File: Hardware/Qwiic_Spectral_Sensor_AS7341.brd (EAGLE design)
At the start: 25.4 x 25.4 mm, 43 parts, among them J1 QWIIC_RIGHT_ANGLE, J3 QWIIC_RIGHT_ANGLE, U1 MLX90614

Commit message: Working on schematic
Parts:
- removed R5: 2.2k, SparkFun-Resistors:0603
- added C2: 0.1uF, SparkFun-Capacitors:0603
- added C3, C4: 1.0uF, SparkFun-Capacitors:0603
- added D2: White, 60mA, SparkFun-LED:SUPER_BRIGHT_SMD_LED_3014
- added D3: LED-IR0603, SparkFun-LED:LED-0603
- added D4, D5: (no value), SparkFun-LED:LED_3MM-NS
- added JP3, JP4: JUMPER-SMT_2_NC_TRACE_SILK, SparkFun-Jumpers:SMT-JUMPER_2_NC_TRACE_SILK
- added R1: 2.2k, SparkFun-Resistors:0603
- added U2: PCA9536, New_Parts:MSOP8
- added U3: AP2127K-1.8V, SparkFun-IC-Power:SOT23-5
- C1: value 0.1uF -> 10uF
- U1: value MLX90614 -> AS7341OLGA; device SparkFun-Sensors:TO-39 -> AS7341:OLGA8
- moved R2 54.4 mm to (-14.0, -26.7)
- moved JP1 48.5 mm to (-8.89, -17.8), flipped to the top, turned to 0 degrees
- moved C1 25.6 mm to (-3.81, -15.2), turned to 0 degrees
- moved U1 24.3 mm to (-3.81, -5.08)
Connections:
- new net 1.8V: C4.1, U1.1, U3.5
- new net GPIO0: U2.1
- new net GPIO1: U2.2
- new net GPIO2: U2.3
- new net GPIO3: U2.5
- new net LDR: D2.C, D3.C, D4.K, D5.K, U1.4
- new net N$5: D2.A, JP4.1
- new net N$6: U3.1, U3.3
- new net N$7: D3.A, JP3.1
- net 3.3V: now also C2.1, C3.1, U2.8; no longer U1.3
- net GND: now also C2.2, C3.2, C4.2, U1.3, U1.5, U2.4, U3.2; no longer U1.4
- net N$1: now also JP1.3, R1.1; no longer JP1.1, R2.2
- net N$3: now also JP1.1, R2.1; no longer JP1.3, R5.2
- net SCL: now also R2.2, U1.2, U2.6; no longer R2.1, U1.1
- net SDA: now also R1.2, U1.8, U2.7; no longer R5.1, U1.2
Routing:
- net 3.3V: track 48.2 -> 31.1 mm
- net SDA: track 38.4 -> 29.1 mm
- net SCL: track 44.4 -> 39.4 mm
- net N$1: track 4.36 -> 0.00 mm, vias 1 -> 0
- net N$3: track 4.32 -> 0.00 mm, vias 1 -> 0

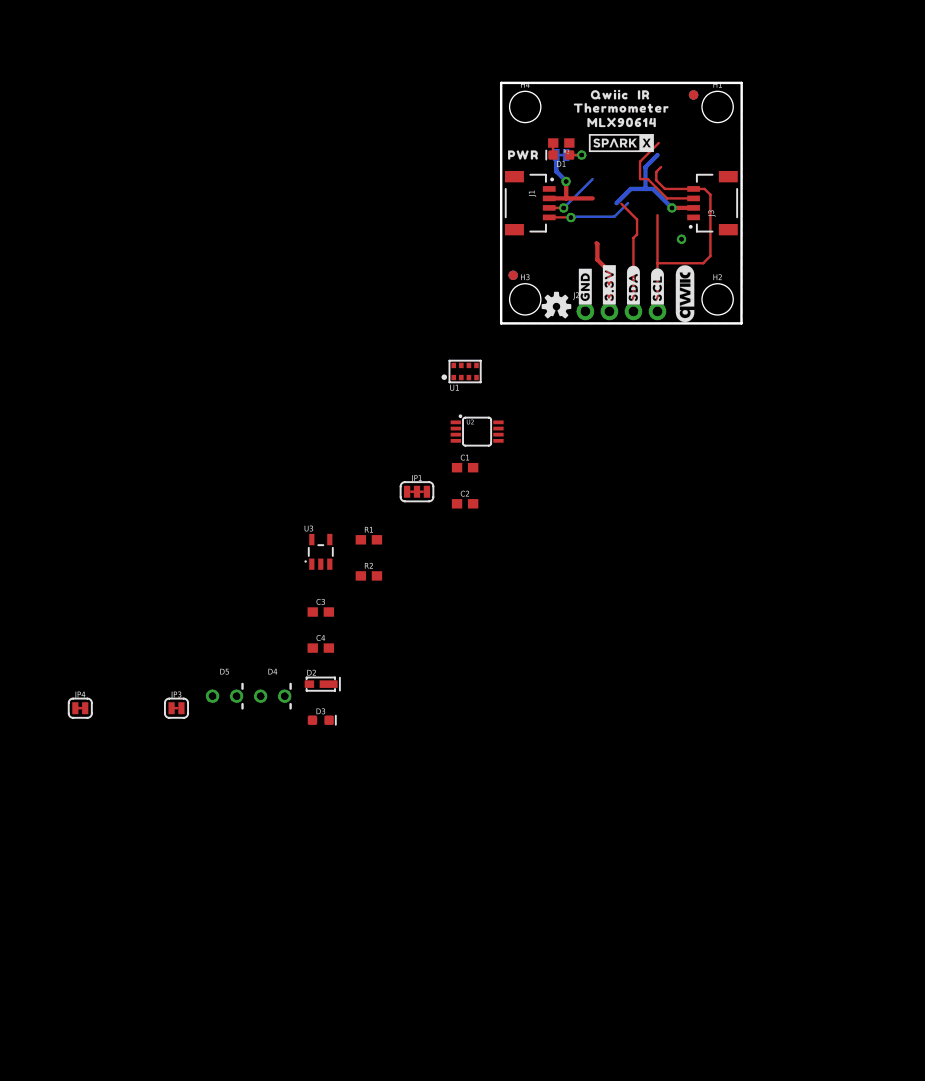
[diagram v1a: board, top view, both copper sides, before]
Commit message: First draft of schematic finished
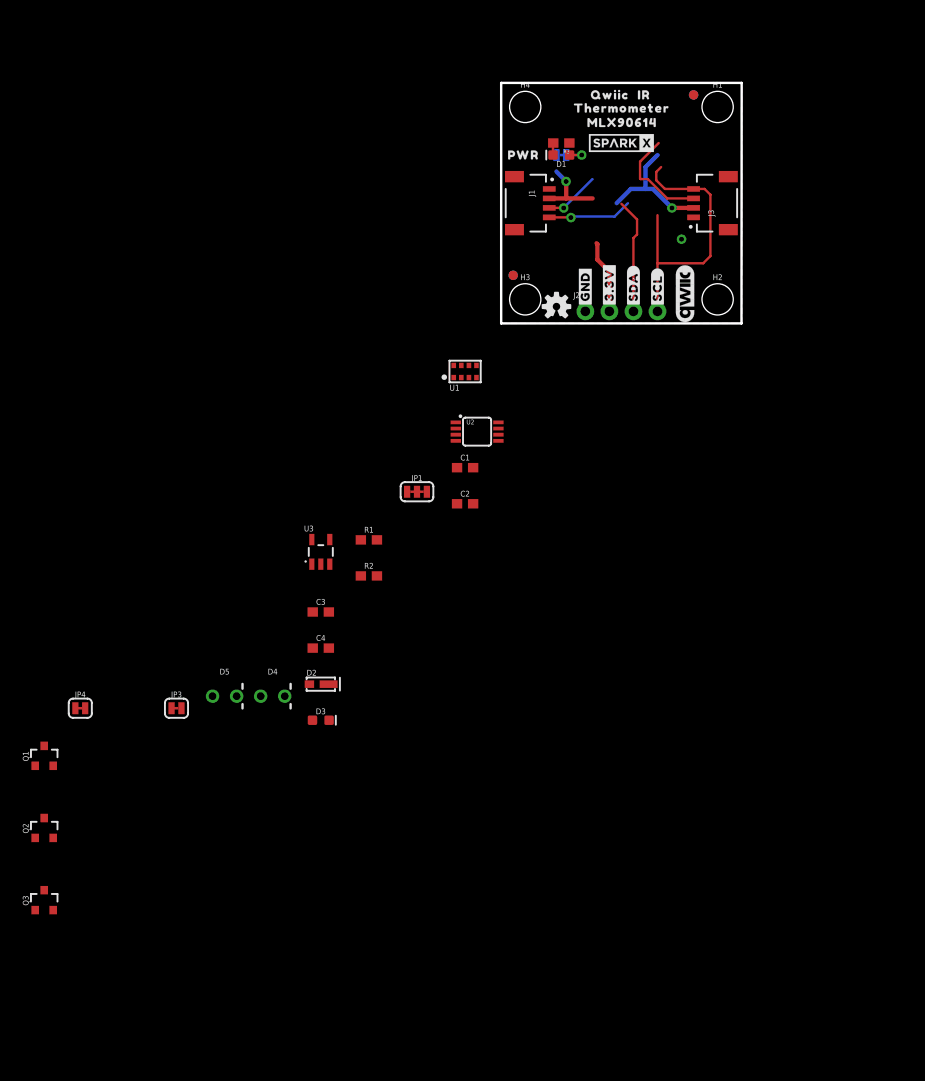
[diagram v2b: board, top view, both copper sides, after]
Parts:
- added Q1, Q2, Q3: 20V/4.2A/52mΩ/1.4W, SparkFun-DiscreteSemi:SOT23-3
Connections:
- new net N$10: JP2.2, Q3.2
- new net N$8: D4.A, JP4.2, Q1.2
- new net N$9: D5.A, JP3.2, Q2.2
- net 3.3V: now also Q1.3, Q2.3, Q3.3; no longer JP2.2
- net GPIO0: now also Q3.1
- net GPIO1: now also Q1.1
- net GPIO2: now also Q2.1
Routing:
- net 3.3V: track 31.1 -> 29.3 mm
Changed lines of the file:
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@@
 <attribute name="VALUE" x="-44.45" y="-41.783" size="0.6096" layer="27" font="vector" ratio="20" align="top-center"/>
+</element>
+<element name="Q1" library="SparkFun-DiscreteSemi" package="SOT23-3" value="20V/4.2A/52mΩ/1.4W" x="-48.26" y="-45.72" smashed="yes">
+<attribute name="NAME" x="-49.911" y="-45.72" size="0.6096" layer="25" font="vector" ratio="20" rot="R90" align="bottom-center"/>
+<attribute name="PROD_ID" value="TRAN-14388" x="-48.26" y="-45.72" size="1.778" layer="27" font="vector" ratio="15" display="off"/>
+<attribute name="VALUE" x="-46.609" y="-45.72" size="0.6096" layer="27" font="vector" ratio="20" rot="R90" align="top-center"/>
+</element>
+<element name="Q2" library="SparkFun-DiscreteSemi" package="SOT23-3" value="20V/4.2A/52mΩ/1.4W" x="-48.26" y="-53.34" smashed="yes">
+<attribute name="NAME" x="-49.911" y="-53.34" size="0.6096" layer="25" font="vector" ratio="20" rot="R90" align="bottom-center"/>
+<attribute name="PROD_ID" value="TRAN-14388" x="-48.26" y="-53.34" size="1.778" layer="27" font="vector" ratio="15" display="off"/>
+<attribute name="VALUE" x="-46.609" y="-53.34" size="0.6096" layer="27" font="vector" ratio="20" rot="R90" align="top-center"/>
+</element>
+<element name="Q3" library="SparkFun-DiscreteSemi" package="SOT23-3" value="20V/4.2A/52mΩ/1.4W" x="-48.26" y="-60.96" smashed="yes">
+<attribute name="NAME" x="-49.911" y="-60.96" size="0.6096" layer="25" font="vector" ratio="20" rot="R90" align="bottom-center"/>
+<attribute name="PROD_ID" value="TRAN-14388" x="-48.26" y="-60.96" size="1.778" layer="27" font="vector" ratio="15" display="off"/>
+<attribute name="VALUE" x="-46.609" y="-60.96" size="0.6096" layer="27" font="vector" ratio="20" rot="R90" align="top-center"/>
 </element>
 </elements>
@@
 <wire x1="6.8707" y1="14.9733" x2="6.8707" y2="13.2127" width="0.4572" layer="1"/>
 <wire x1="10.16" y1="6.731" x2="10.16" y2="8.382" width="0.4572" layer="1"/>
-<contactref element="JP2" pad="2"/>
 <wire x1="10.072" y1="8.47" x2="10.16" y2="8.382" width="0.4572" layer="1"/>
 <wire x1="16.51" y1="17.78" x2="15.24" y2="16.51" width="0.4572" layer="16"/>
 <wire x1="15.24" y1="16.51" x2="15.24" y2="14.1986" width="0.4572" layer="16"/>
-<wire x1="5.8293" y1="17.78" x2="5.8293" y2="16.0401" width="0.4572" layer="16"/>
 <wire x1="5.8293" y1="16.0401" x2="6.8707" y2="14.9987" width="0.4572" layer="16"/>
 <contactref element="U2" pad="8"/>
@@
 <contactref element="JP1" pad="2"/>
 <contactref element="C3" pad="1"/>
+<contactref element="Q1" pad="3"/>
+<contactref element="Q2" pad="3"/>
+<contactref element="Q3" pad="3"/>
+<wire x1="-48.26" y1="-52.24" x2="-48.26" y2="-59.86" width="0" layer="19" extent="1-1"/>
+<wire x1="-48.26" y1="-44.62" x2="-48.26" y2="-52.24" width="0" layer="19" extent="1-1"/>
+<wire x1="-19.9" y1="-30.48" x2="-48.26" y2="-44.62" width="0" layer="19" extent="1-1"/>
 <wire x1="-8.89" y1="-17.78" x2="-19.9" y2="-30.48" width="0" layer="19" extent="1-1"/>
 <wire x1="-4.66" y1="-19.05" x2="-8.89" y2="-17.78" width="0" layer="19" extent="1-1"/>
@@
 <signal name="GPIO0">
 <contactref element="U2" pad="1"/>
+<contactref element="Q3" pad="1"/>
+<wire x1="-4.79" y1="-10.455" x2="-49.21" y2="-61.96" width="0" layer="19" extent="1-1"/>
 </signal>
 <signal name="GPIO1">
 <contactref element="U2" pad="2"/>
+<contactref element="Q1" pad="1"/>
+<wire x1="-4.79" y1="-11.105" x2="-49.21" y2="-46.72" width="0" layer="19" extent="1-1"/>
 </signal>
 <signal name="GPIO2">
 <contactref element="U2" pad="3"/>
+<contactref element="Q2" pad="1"/>
+<wire x1="-4.79" y1="-11.755" x2="-49.21" y2="-54.34" width="0" layer="19" extent="1-1"/>
 </signal>
 <signal name="GPIO3">
@@
 <wire x1="-19.927" y1="-41.91" x2="-34.8107" y2="-40.64" width="0" layer="19" extent="1-1"/>
 </signal>
+<signal name="N$8">
+<contactref element="D4" pad="A"/>
+<contactref element="Q1" pad="2"/>
+<contactref element="JP4" pad="2"/>
+<wire x1="-43.9293" y1="-40.64" x2="-47.31" y2="-46.72" width="0" layer="19" extent="1-1"/>
+<wire x1="-25.4" y1="-39.37" x2="-43.9293" y2="-40.64" width="0" layer="19" extent="1-1"/>
+</signal>
+<signal name="N$9">
+<contactref element="D5" pad="A"/>
+<contactref element="Q2" pad="2"/>
+<contactref element="JP3" pad="2"/>
+<wire x1="-33.7693" y1="-40.64" x2="-47.31" y2="-54.34" width="0" layer="19" extent="1-1"/>
+<wire x1="-30.48" y1="-39.37" x2="-33.7693" y2="-40.64" width="0" layer="19" extent="1-1"/>
+</signal>
+<signal name="N$10">
+<contactref element="JP2" pad="2"/>
+<contactref element="Q3" pad="2"/>
+<wire x1="5.8293" y1="17.78" x2="-47.31" y2="-61.96" width="0" layer="19" extent="1-16"/>
+</signal>
 </signals>

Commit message: Added int pin to schematic
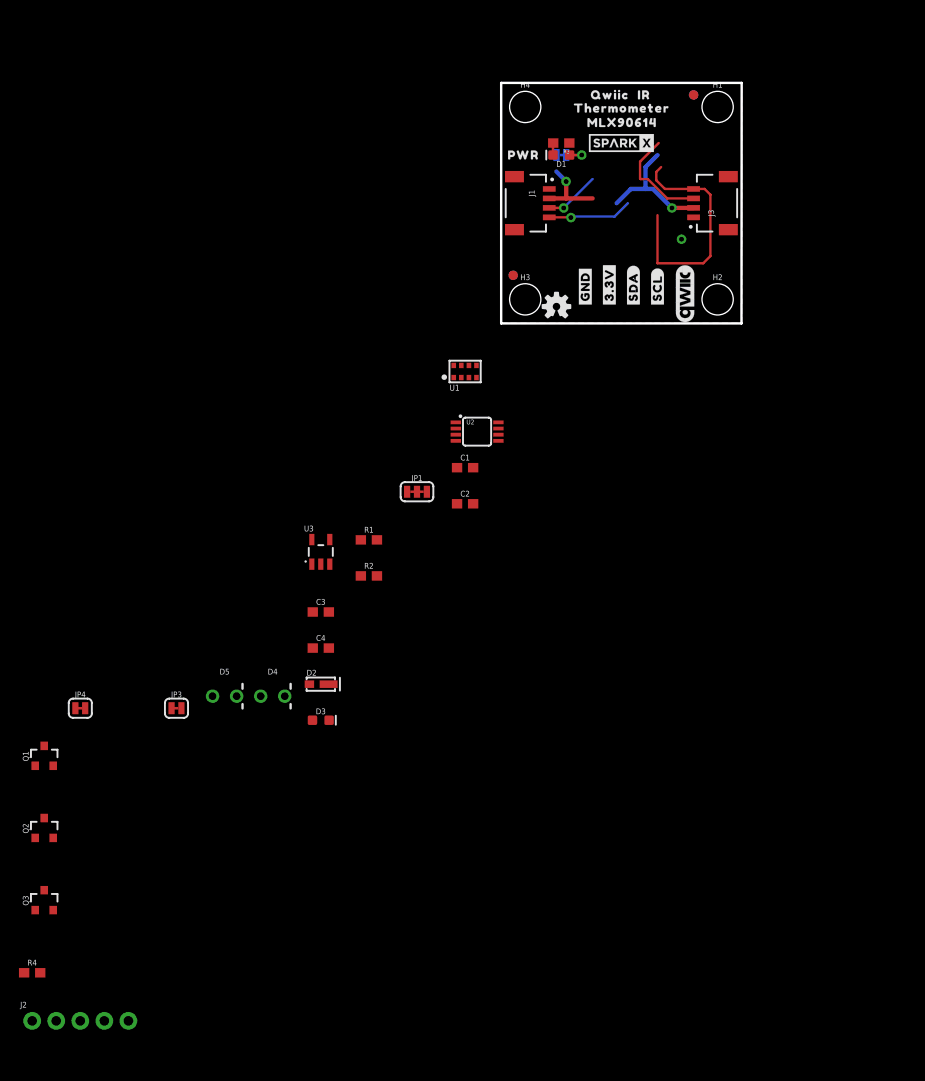
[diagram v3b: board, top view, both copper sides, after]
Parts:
- added R4: 2.2k, SparkFun-Resistors:0603
- J2: device SparkFun-Connectors:1X04_NO_SILK -> SparkFun-Connectors:1X05_NO_SILK
- moved J2 95.0 mm to (-49.5, -73.7)
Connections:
- new net INT: J2.5, R4.1, U1.7
- net 1.8V: now also R4.2
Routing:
- net SDA: track 29.1 -> 16.9 mm
- net 3.3V: track 29.3 -> 21.6 mm
- net SCL: track 39.4 -> 34.4 mm
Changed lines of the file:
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@@
 <attribute name="VALUE" x="1.778" y="14.351" size="0.6096" layer="27" font="vector" ratio="20" rot="R270"/>
-</element>
-<element name="J2" library="SparkFun-Connectors" package="1X04_NO_SILK" value="" x="8.89" y="1.27" smashed="yes">
-<attribute name="NAME" x="7.62" y="2.667" size="0.6096" layer="25" font="vector" ratio="20"/>
-<attribute name="VALUE" x="7.62" y="-0.762" size="0.6096" layer="27" font="vector" ratio="20"/>
 </element>
 <element name="JP2" library="SparkFun-Jumpers" package="SMT-JUMPER_2_NC_TRACE_SILK" package3d_urn="urn:adsk.eagle:package:39281/1" value="JUMPER-SMT_2_NC_TRACE_SILK" x="6.35" y="17.78" smashed="yes" rot="MR0">
@@
 <attribute name="VALUE" x="-46.609" y="-60.96" size="0.6096" layer="27" font="vector" ratio="20" rot="R90" align="top-center"/>
 </element>
+<element name="R4" library="SparkFun-Resistors" package="0603" value="2.2k" x="-49.53" y="-68.58" smashed="yes">
+<attribute name="NAME" x="-49.53" y="-67.818" size="0.6096" layer="25" font="vector" ratio="20" align="bottom-center"/>
+<attribute name="PROD_ID" value="RES-08272" x="-49.53" y="-68.58" size="1.778" layer="27" font="vector" ratio="15" display="off"/>
+<attribute name="VALUE" x="-49.53" y="-69.342" size="0.6096" layer="27" font="vector" ratio="20" align="top-center"/>
+</element>
+<element name="J2" library="SparkFun-Connectors" package="1X05_NO_SILK" value="" x="-49.53" y="-73.66" smashed="yes">
+<attribute name="NAME" x="-50.8" y="-72.263" size="0.6096" layer="25" font="vector" ratio="20"/>
+<attribute name="VALUE" x="-50.8" y="-75.692" size="0.6096" layer="27" font="vector" ratio="20"/>
+</element>
 </elements>
 <signals>
 <signal name="3.3V">
 <contactref element="J1" pad="2"/>
-<contactref element="J2" pad="2"/>
 <contactref element="J3" pad="2"/>
-<wire x1="11.43" y1="5.461" x2="10.16" y2="6.731" width="0.4572" layer="1"/>
-<wire x1="11.43" y1="5.461" x2="11.43" y2="1.27" width="0.4572" layer="1"/>
 <wire x1="5.08" y1="13.2" x2="6.858" y2="13.2" width="0.4572" layer="1"/>
 <wire x1="9.66" y1="13.2" x2="6.858" y2="13.2" width="0.4572" layer="1"/>
@@
 <wire x1="6.858" y1="14.986" x2="6.8707" y2="14.9733" width="0.4572" layer="1"/>
 <wire x1="6.8707" y1="14.9733" x2="6.8707" y2="13.2127" width="0.4572" layer="1"/>
-<wire x1="10.16" y1="6.731" x2="10.16" y2="8.382" width="0.4572" layer="1"/>
-<wire x1="10.072" y1="8.47" x2="10.16" y2="8.382" width="0.4572" layer="1"/>
 <wire x1="16.51" y1="17.78" x2="15.24" y2="16.51" width="0.4572" layer="16"/>
 <wire x1="15.24" y1="16.51" x2="15.24" y2="14.1986" width="0.4572" layer="16"/>
@@
 <contactref element="Q2" pad="3"/>
 <contactref element="Q3" pad="3"/>
+<contactref element="J2" pad="2"/>
+<wire x1="-48.26" y1="-59.86" x2="-46.99" y2="-73.66" width="0" layer="19" extent="1-1"/>
 <wire x1="-48.26" y1="-52.24" x2="-48.26" y2="-59.86" width="0" layer="19" extent="1-1"/>
 <wire x1="-48.26" y1="-44.62" x2="-48.26" y2="-52.24" width="0" layer="19" extent="1-1"/>
@@
 <wire x1="-4.66" y1="-15.24" x2="-4.66" y2="-19.05" width="0" layer="19" extent="1-1"/>
 <wire x1="-0.29" y1="-10.455" x2="-4.66" y2="-15.24" width="0" layer="19" extent="1-1"/>
-<wire x1="11.43" y1="1.27" x2="-0.29" y2="-10.455" width="0" layer="19" extent="1-1"/>
-<wire x1="12.192" y1="12.7" x2="10.072" y2="8.47" width="0" layer="19" extent="1-16"/>
-<wire x1="9.66" y1="13.2" x2="12.192" y2="12.7" width="0" layer="19" extent="1-16"/>
+<wire x1="5.08" y1="13.2" x2="-0.29" y2="-10.455" width="0" layer="19" extent="1-1"/>
+<wire x1="12.192" y1="12.7" x2="9.66" y2="13.2" width="0" layer="19" extent="1-16"/>
 </signal>
 <signal name="SDA">
 <contactref element="J1" pad="3"/>
-<contactref element="J2" pad="3"/>
 <contactref element="J3" pad="3"/>
 <wire x1="17.534" y1="13.2" x2="20.32" y2="13.2" width="0.254" layer="1"/>
 <wire x1="15.494" y1="15.24" x2="17.534" y2="13.2" width="0.254" layer="1"/>
-<wire x1="14.351" y1="10.975975" x2="12.7" y2="12.626975" width="0.254" layer="1"/>
-<wire x1="13.97" y1="1.27" x2="13.97" y2="9.017" width="0.254" layer="1"/>
-<wire x1="13.97" y1="9.017" x2="14.351" y2="9.398" width="0.254" layer="1"/>
-<wire x1="14.351" y1="9.398" x2="14.351" y2="10.975975" width="0.254" layer="1"/>
 <wire x1="5.08" y1="12.2" x2="6.596" y2="12.2" width="0.254" layer="1"/>
 <wire x1="6.596" y1="12.2" x2="6.604" y2="12.192" width="0.254" layer="1"/>
@@
 <contactref element="U2" pad="7"/>
 <contactref element="R1" pad="2"/>
+<contactref element="J2" pad="3"/>
+<wire x1="-13.12" y1="-22.86" x2="-44.45" y2="-73.66" width="0" layer="19" extent="1-1"/>
 <wire x1="-0.29" y1="-11.105" x2="-13.12" y2="-22.86" width="0" layer="19" extent="1-1"/>
 <wire x1="-5.01" y1="-4.442" x2="-0.29" y2="-11.105" width="0" layer="19" extent="1-1"/>
-<wire x1="13.97" y1="1.27" x2="-0.29" y2="-11.105" width="0" layer="19" extent="1-1"/>
-<wire x1="9.652" y1="15.24" x2="12.7" y2="12.626975" width="0" layer="19" extent="1-16"/>
-<wire x1="16.637" y1="19.05" x2="12.7" y2="12.626975" width="0" layer="19" extent="1-1"/>
+<wire x1="5.08" y1="12.2" x2="-5.01" y2="-4.442" width="0" layer="19" extent="1-1"/>
+<wire x1="16.637" y1="19.05" x2="9.652" y2="15.24" width="0" layer="19" extent="1-16"/>
 </signal>
 <signal name="SCL">
 <contactref element="J1" pad="4"/>
-<contactref element="J2" pad="4"/>
 <contactref element="J3" pad="4"/>
 <wire x1="16.51" y1="6.35" x2="16.51" y2="11.43" width="0.254" layer="1"/>
-<wire x1="16.51" y1="6.35" x2="16.51" y2="1.27" width="0.254" layer="1"/>
 <wire x1="20.32" y1="14.2" x2="21.487" y2="14.2" width="0.254" layer="1"/>
 <wire x1="21.487" y1="14.2" x2="22.098" y2="13.589" width="0.254" layer="1"/>
@@
 <contactref element="U2" pad="6"/>
 <contactref element="R2" pad="2"/>
+<contactref element="J2" pad="4"/>
+<wire x1="-13.12" y1="-26.67" x2="-41.91" y2="-73.66" width="0" layer="19" extent="1-1"/>
 <wire x1="-0.29" y1="-11.755" x2="-13.12" y2="-26.67" width="0" layer="19" extent="1-1"/>
 <wire x1="-4.21" y1="-5.718" x2="-0.29" y2="-11.755" width="0" layer="19" extent="1-1"/>
@@
 </polygon>
 <contactref element="J1" pad="1"/>
-<contactref element="J2" pad="1"/>
 <contactref element="J3" pad="1"/>
 <via x="19.05" y="8.89" extent="1-16" drill="0.508"/>
@@
 <contactref element="C3" pad="2"/>
 <contactref element="C4" pad="2"/>
+<contactref element="J2" pad="1"/>
+<wire x1="-18.2" y1="-34.29" x2="-49.53" y2="-73.66" width="0" layer="19" extent="1-1"/>
 <wire x1="-18.2" y1="-30.48" x2="-18.2" y2="-34.29" width="0" layer="19" extent="1-1"/>
 <wire x1="-19.05" y1="-25.4301" x2="-18.2" y2="-30.48" width="0" layer="19" extent="1-1"/>
@@
 <wire x1="-3.41" y1="-5.718" x2="-4.79" y2="-12.405" width="0" layer="19" extent="1-1"/>
 <wire x1="-2.61" y1="-4.442" x2="-3.41" y2="-5.718" width="0" layer="19" extent="1-1"/>
-<wire x1="8.89" y1="1.27" x2="-2.61" y2="-4.442" width="0" layer="19" extent="1-1"/>
-<wire x1="19.05" y1="8.89" x2="8.89" y2="1.27" width="0" layer="19" extent="1-1"/>
+<wire x1="5.08" y1="14.2" x2="-2.61" y2="-4.442" width="0" layer="19" extent="1-1"/>
+<wire x1="7.2" y1="19.05" x2="5.08" y2="14.2" width="0" layer="19" extent="1-1"/>
+<wire x1="19.05" y1="8.89" x2="5.08" y2="14.2" width="0" layer="19" extent="1-1"/>
 <wire x1="20.32" y1="11.2" x2="19.05" y2="8.89" width="0" layer="19" extent="1-1"/>
-<wire x1="5.08" y1="14.2" x2="8.89" y2="1.27" width="0" layer="19" extent="1-1"/>
-<wire x1="7.2" y1="19.05" x2="5.08" y2="14.2" width="0" layer="19" extent="1-1"/>
 </signal>
 <signal name="N$4">
@@
 <contactref element="U1" pad="1"/>
 <contactref element="C4" pad="1"/>
+<contactref element="R4" pad="2"/>
+<wire x1="-19.9" y1="-34.29" x2="-48.68" y2="-68.58" width="0" layer="19" extent="1-1"/>
 <wire x1="-20" y1="-22.8299" x2="-19.9" y2="-34.29" width="0" layer="19" extent="1-1"/>
 <wire x1="-5.01" y1="-5.718" x2="-20" y2="-22.8299" width="0" layer="19" extent="1-1"/>
@@
 <wire x1="5.8293" y1="17.78" x2="-47.31" y2="-61.96" width="0" layer="19" extent="1-16"/>
 </signal>
+<signal name="INT">
+<contactref element="U1" pad="7"/>
+<contactref element="R4" pad="1"/>
+<contactref element="J2" pad="5"/>
+<wire x1="-39.37" y1="-73.66" x2="-50.38" y2="-68.58" width="0" layer="19" extent="1-1"/>
+<wire x1="-4.21" y1="-4.442" x2="-39.37" y2="-73.66" width="0" layer="19" extent="1-1"/>
+</signal>
 </signals>
